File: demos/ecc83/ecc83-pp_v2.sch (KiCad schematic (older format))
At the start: 15 parts, among them P1 IN, P2 OUT, P3 POWER, P4 CONN_2, P5 CONN_1, P6 CONN_1, P7 CONN_1, P8 CONN_1, U1 ECC83

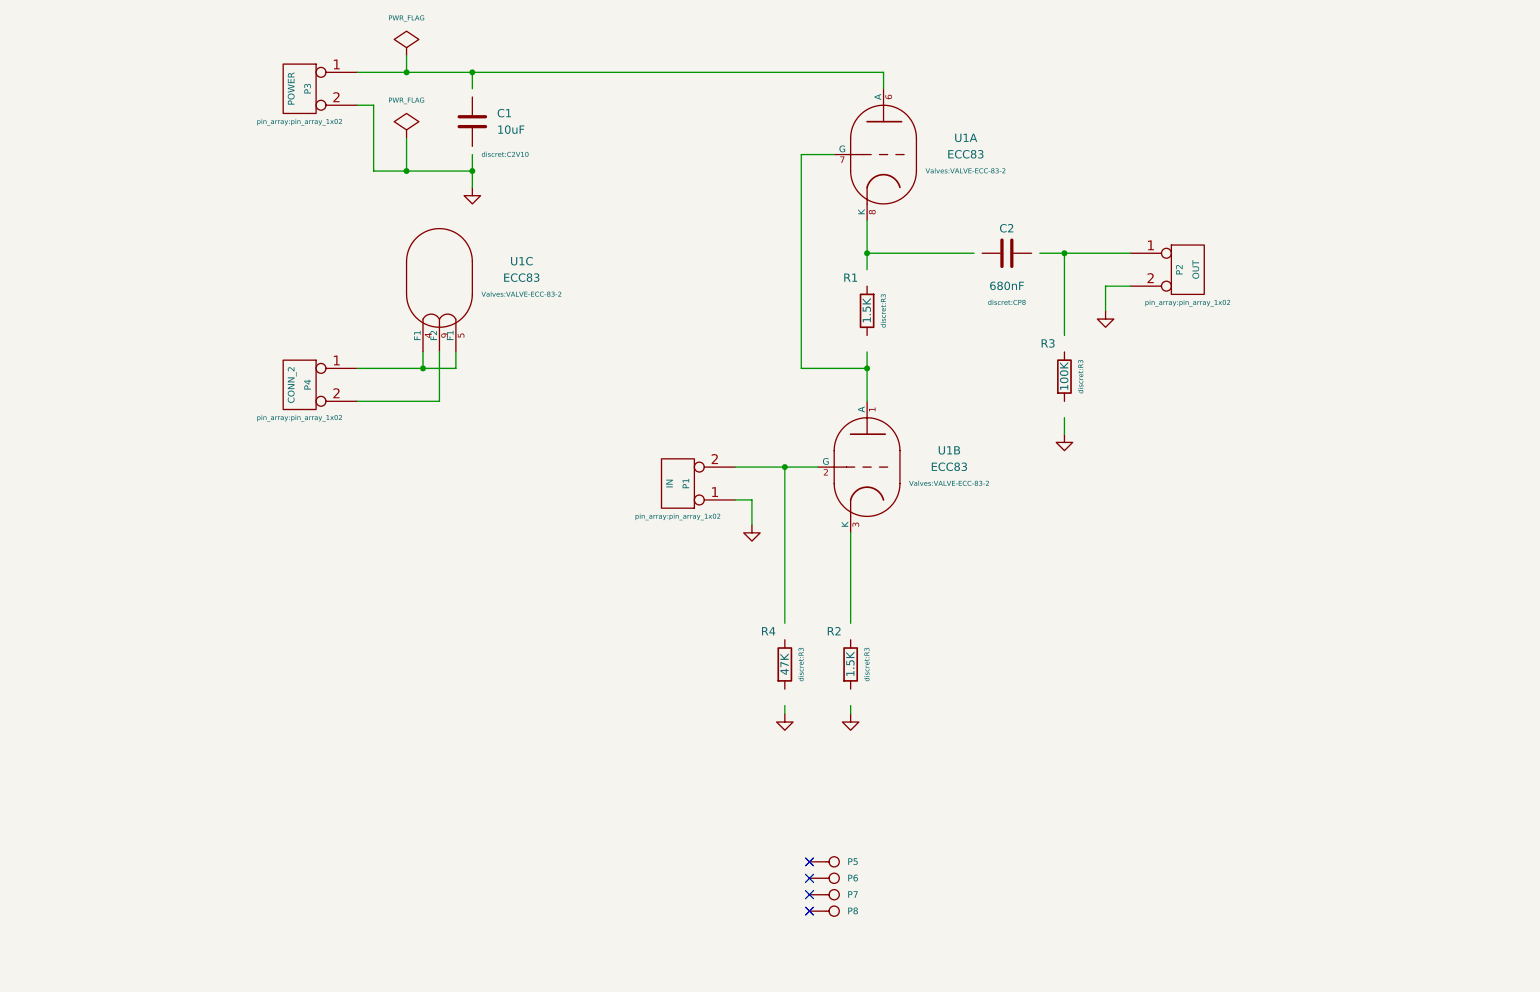
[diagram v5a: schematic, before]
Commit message: Demos: make a private library for each demo, to avoid issues when using modified kicad new schematic libraries
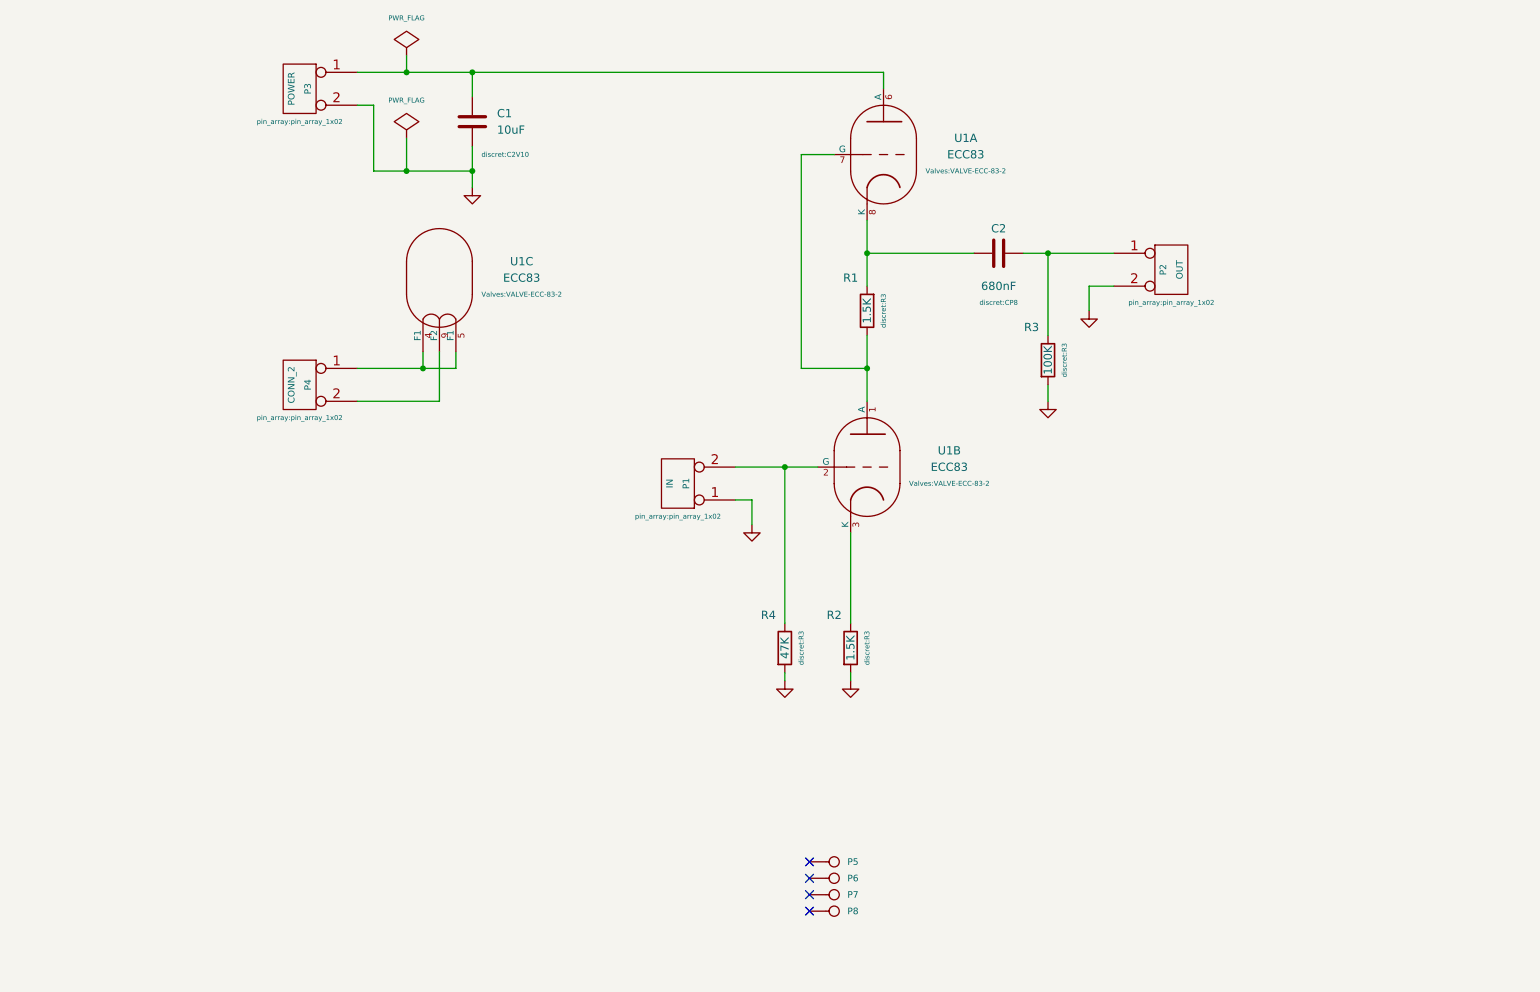
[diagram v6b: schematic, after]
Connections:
- wire segments 41 -> 32
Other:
- moved on the sheet: C2, P2, R2, R3, R4
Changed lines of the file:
@@
 EESchema Schematic File Version 2
+LIBS:ecc83_schlib
 LIBS:power
-LIBS:device
-LIBS:conn
-LIBS:valves
-LIBS:linear
-LIBS:regul
-LIBS:74xx
-LIBS:cmos4000
-LIBS:adc-dac
-LIBS:memory
-LIBS:xilinx
-LIBS:special
-LIBS:microcontrollers
-LIBS:microchip
-LIBS:analog_switches
-LIBS:motorola
-LIBS:intel
-LIBS:audio
-LIBS:interface
-LIBS:digital-audio
-LIBS:philips
-LIBS:display
-LIBS:cypress
-LIBS:siliconi
-LIBS:contrib
 LIBS:ecc83-pp_v2-cache
 EELAYER 25 0
@@
 L GND #PWR01
 U 1 1 457DBAF8
-P 7950 3250
-F 0 "#PWR01" H 7950 3250 30  0001 C CNN
-F 1 "GND" H 7950 3180 30  0001 C CNN
-F 2 "" H 7950 3250 60  0001 C CNN
-F 3 "" H 7950 3250 60  0001 C CNN
-	1    7950 3250
+P 7850 3250
+F 0 "#PWR01" H 7850 3250 30  0001 C CNN
+F 1 "GND" H 7850 3180 30  0001 C CNN
+F 2 "" H 7850 3250 60  0001 C CNN
+F 3 "" H 7850 3250 60  0001 C CNN
+	1    7850 3250
 	1    0    0    -1
 $EndComp
@@
 L GND #PWR02
 U 1 1 457DBAF5
-P 7700 4000
-F 0 "#PWR02" H 7700 4000 30  0001 C CNN
-F 1 "GND" H 7700 3930 30  0001 C CNN
-F 2 "" H 7700 4000 60  0001 C CNN
-F 3 "" H 7700 4000 60  0001 C CNN
-	1    7700 4000
+P 7600 3800
+F 0 "#PWR02" H 7600 3800 30  0001 C CNN
+F 1 "GND" H 7600 3730 30  0001 C CNN
+F 2 "" H 7600 3800 60  0001 C CNN
+F 3 "" H 7600 3800 60  0001 C CNN
+	1    7600 3800
 	1    0    0    -1
 $EndComp
@@
 L GND #PWR03
 U 1 1 457DBAF1
-P 6400 5700
-F 0 "#PWR03" H 6400 5700 30  0001 C CNN
-F 1 "GND" H 6400 5630 30  0001 C CNN
-F 2 "" H 6400 5700 60  0001 C CNN
-F 3 "" H 6400 5700 60  0001 C CNN
-	1    6400 5700
+P 6400 5500
+F 0 "#PWR03" H 6400 5500 30  0001 C CNN
+F 1 "GND" H 6400 5430 30  0001 C CNN
+F 2 "" H 6400 5500 60  0001 C CNN
+F 3 "" H 6400 5500 60  0001 C CNN
+	1    6400 5500
 	1    0    0    -1
 $EndComp
@@
 L GND #PWR04
 U 1 1 457DBAEF
-P 6000 5700
-F 0 "#PWR04" H 6000 5700 30  0001 C CNN
-F 1 "GND" H 6000 5630 30  0001 C CNN
-F 2 "" H 6000 5700 60  0001 C CNN
-F 3 "" H 6000 5700 60  0001 C CNN
-	1    6000 5700
+P 6000 5500
+F 0 "#PWR04" H 6000 5500 30  0001 C CNN
+F 1 "GND" H 6000 5430 30  0001 C CNN
+F 2 "" H 6000 5500 60  0001 C CNN
+F 3 "" H 6000 5500 60  0001 C CNN
+	1    6000 5500
 	1    0    0    -1
 $EndComp
@@
 L CONN_2 P2
 U 1 1 4549F46C
-P 8450 3000
-F 0 "P2" V 8400 3000 40  0000 C CNN
-F 1 "OUT" V 8500 3000 40  0000 C CNN
-F 2 "pin_array:pin_array_1x02" H 8450 2800 30  0000 C CNN
-F 3 "" H 8450 3000 60  0001 C CNN
-	1    8450 3000
+P 8350 3000
+F 0 "P2" V 8300 3000 40  0000 C CNN
+F 1 "OUT" V 8400 3000 40  0000 C CNN
+F 2 "pin_array:pin_array_1x02" H 8350 2800 30  0000 C CNN
+F 3 "" H 8350 3000 60  0001 C CNN
+	1    8350 3000
 	1    0    0    -1
 $EndComp
@@
 L C C2
 U 1 1 4549F3BE
-P 7350 2900
-F 0 "C2" V 7200 2900 50  0000 C CNN
-F 1 "680nF" V 7550 2900 50  0000 C CNN
-F 2 "discret:CP8" V 7650 2900 30  0000 C CNN
-F 3 "" H 7350 2900 60  0001 C CNN
-	1    7350 2900
+P 7300 2900
+F 0 "C2" V 7150 2900 50  0000 C CNN
+F 1 "680nF" V 7500 2900 50  0000 C CNN
+F 2 "discret:CP8" V 7600 2900 30  0000 C CNN
+F 3 "" H 7300 2900 60  0001 C CNN
+	1    7300 2900
 	0    1    1    0
 $EndComp
@@
 L R R3
 U 1 1 4549F3AD
-P 7700 3650
-F 0 "R3" H 7600 3850 50  0000 C CNN
-F 1 "100K" V 7700 3650 50  0000 C CNN
-F 2 "discret:R3" V 7800 3650 30  0000 C CNN
-F 3 "" H 7700 3650 60  0001 C CNN
-	1    7700 3650
+P 7600 3550
+F 0 "R3" H 7500 3750 50  0000 C CNN
+F 1 "100K" V 7600 3550 50  0000 C CNN
+F 2 "discret:R3" V 7700 3550 30  0000 C CNN
+F 3 "" H 7600 3550 60  0001 C CNN
+	1    7600 3550
 	1    0    0    -1
 $EndComp
@@
 L R R4
 U 1 1 4549F3A2
-P 6000 5400
-F 0 "R4" H 5900 5600 50  0000 C CNN
-F 1 "47K" V 6000 5400 50  0000 C CNN
-F 2 "discret:R3" V 6100 5400 30  0000 C CNN
-F 3 "" H 6000 5400 60  0001 C CNN
-	1    6000 5400
+P 6000 5300
+F 0 "R4" H 5900 5500 50  0000 C CNN
+F 1 "47K" V 6000 5300 50  0000 C CNN
+F 2 "discret:R3" V 6100 5300 30  0000 C CNN
+F 3 "" H 6000 5300 60  0001 C CNN
+	1    6000 5300
 	1    0    0    -1
 $EndComp
@@
 L R R2
 U 1 1 4549F39D
-P 6400 5400
-F 0 "R2" H 6300 5600 50  0000 C CNN
-F 1 "1.5K" V 6400 5400 50  0000 C CNN
-F 2 "discret:R3" V 6500 5400 30  0000 C CNN
-F 3 "" H 6400 5400 60  0001 C CNN
-	1    6400 5400
+P 6400 5300
+F 0 "R2" H 6300 5500 50  0000 C CNN
+F 1 "1.5K" V 6400 5300 50  0000 C CNN
+F 2 "discret:R3" V 6500 5300 30  0000 C CNN
+F 3 "" H 6400 5300 60  0001 C CNN
+	1    6400 5300
 	1    0    0    -1
 $EndComp
@@
 NoConn ~ 6150 6900
 $Comp
-L PWR_FLAG #FLG?
+L PWR_FLAG #FLG06
 U 1 1 550E41D9
 P 3700 1700
-F 0 "#FLG?" H 3700 1970 30  0001 C CNN
+F 0 "#FLG06" H 3700 1970 30  0001 C CNN
 F 1 "PWR_FLAG" H 3700 1930 30  0000 C CNN
 F 2 "" H 3700 1700 60  0001 C CNN
@@
 $EndComp
 $Comp
-L GND #PWR?
+L GND #PWR07
 U 1 1 550E42C4
 P 4100 2500
-F 0 "#PWR?" H 4100 2500 30  0001 C CNN
+F 0 "#PWR07" H 4100 2500 30  0001 C CNN
 F 1 "GND" H 4100 2430 30  0001 C CNN
 F 2 "" H 4100 2500 60  0000 C CNN
@@
 	6400 4600 6400 5150
 Wire Wire Line
-	7550 2900 7700 2900
-Wire Wire Line
-	7700 2900 8100 2900
-Wire Wire Line
-	3400 3600 3800 3600
-Wire Wire Line
-	3800 3600 4000 3600
+	7450 2900 8000 2900
+Wire Wire Line
+	3400 3600 4000 3600
 Wire Wire Line
 	3800 3600 3800 3500
 Wire Wire Line
-	6500 3500 6500 3600
-Wire Wire Line
-	6500 3600 6500 3800
+	6500 3400 6500 3800
 Connection ~ 3800 3600
 Wire Wire Line
@@
 Connection ~ 6500 3600
 Wire Wire Line
-	6500 2700 6500 2900
-Wire Wire Line
-	6500 2900 6500 3000
+	6500 2700 6500 3100
 Wire Wire Line
 	6500 3600 6100 3600
@@
 Connection ~ 6500 2900
 Wire Wire Line
-	3400 1800 3700 1800
-Wire Wire Line
-	3700 1800 4100 1800
-Wire Wire Line
-	4100 1800 6600 1800
+	3400 1800 6600 1800
 Wire Wire Line
 	6600 1800 6600 1900
@@
 	3500 2000 3500 2400
 Wire Wire Line
-	3500 2400 3700 2400
-Wire Wire Line
-	3700 2400 4100 2400
+	3500 2400 4100 2400
 Connection ~ 3700 2400
 Wire Wire Line
 	3700 2400 3700 2200
 Wire Wire Line
-	4100 2300 4100 2400
-Wire Wire Line
-	4100 2400 4100 2500
+	4100 2250 4100 2500
 Connection ~ 4100 2400
 Wire Wire Line
-	4100 1900 4100 1800
+	4100 1950 4100 1800
 Connection ~ 4100 1800
 Wire Wire Line
 	6500 2900 7150 2900
-Connection ~ 7700 2900
-Wire Wire Line
-	7700 3900 7700 4000
-Wire Wire Line
-	7700 3400 7700 2900
-Wire Wire Line
-	8100 3100 7950 3100
-Wire Wire Line
-	7950 3100 7950 3250
-Wire Wire Line
-	5700 4200 6000 4200
-Wire Wire Line
-	6000 4200 6200 4200
+Connection ~ 7600 2900
+Wire Wire Line
+	7600 3700 7600 3800
+Wire Wire Line
+	7600 3400 7600 2900
+Wire Wire Line
+	8000 3100 7850 3100
+Wire Wire Line
+	7850 3100 7850 3250
+Wire Wire Line
+	5700 4200 6200 4200
 Wire Wire Line
 	6000 5150 6000 4200
 Connection ~ 6000 4200
 $Comp
-L GND #PWR?
+L GND #PWR08
 U 1 1 550E4C85
 P 5800 4550
-F 0 "#PWR?" H 5800 4550 30  0001 C CNN
+F 0 "#PWR08" H 5800 4550 30  0001 C CNN
 F 1 "GND" H 5800 4480 30  0001 C CNN
 F 2 "" H 5800 4550 60  0000 C CNN
@@
 	5800 4400 5700 4400
 Wire Wire Line
-	6400 5650 6400 5700
-Wire Wire Line
-	6000 5650 6000 5700
+	6400 5450 6400 5500
+Wire Wire Line
+	6000 5450 6000 5500
 $EndSCHEMATC
